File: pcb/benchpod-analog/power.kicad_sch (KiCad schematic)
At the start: 10 parts, among them U30 TPS82130SILR

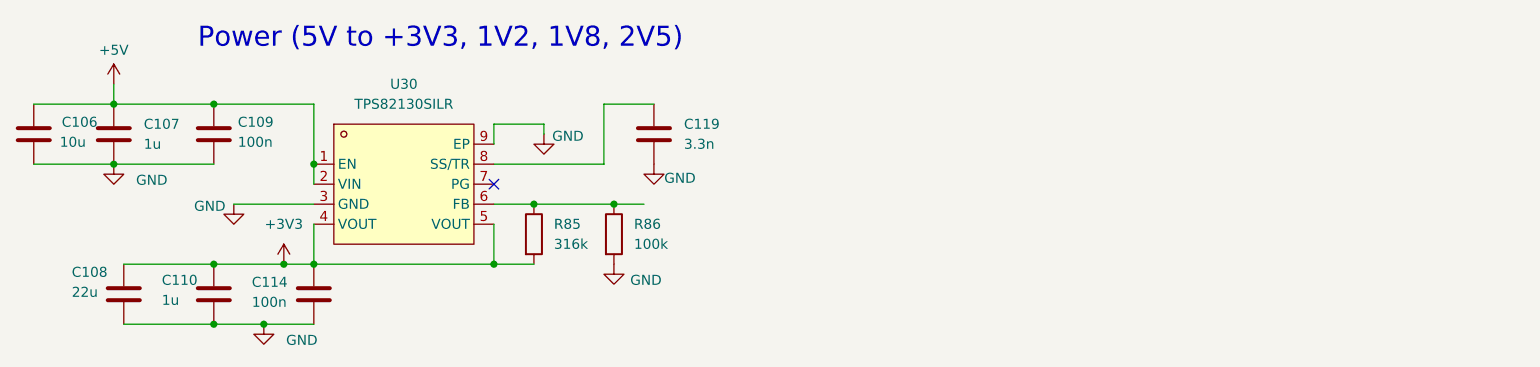
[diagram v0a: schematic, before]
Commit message: analog only board: +3V3 from an AP2112K-3.3 instead of the 3 A buck
On this board +3V3 only feeds logic I/O (DAC8554 IOVDD, MCP33131 DVIO,
TCA9554, the new EEPROM): a few mA. U30 TPS82130 (3 A module) becomes
AP2112K-3.3 (C51118, same part as U46, so no new BOM line): VIN and EN on
+5V, VOUT to +3V3, C107/C109 in, C110/C114 out. R85, R86, C119 and C108
removed. Separate from U46's +3V3A so logic I/O stays off the analog rail.

BOM: TPS82130, 316k and 3.3n lines gone (-3), about $4.75 per board.

Co-Authored-By: Claude Opus 5.5 <noreply@anthropic.com>
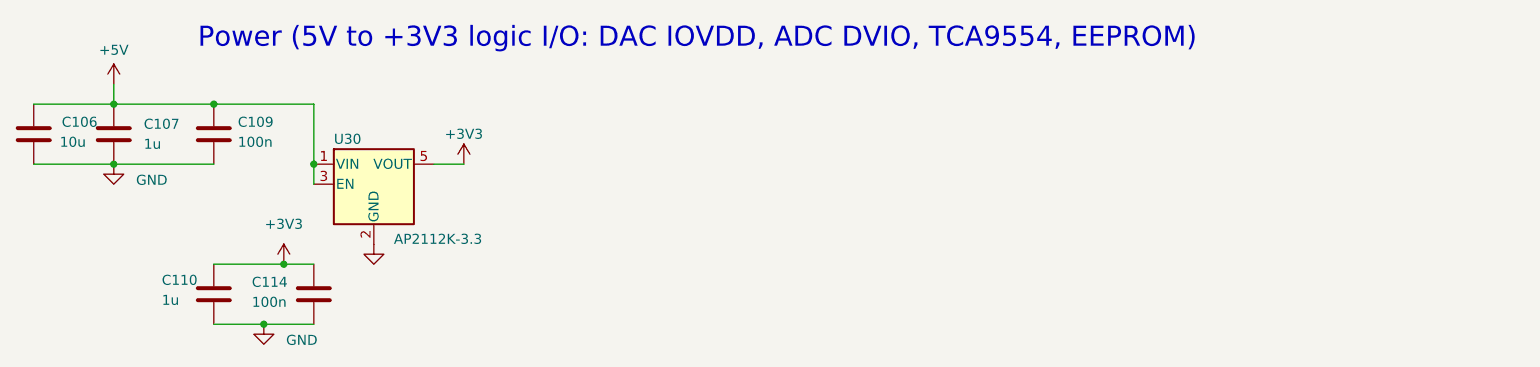
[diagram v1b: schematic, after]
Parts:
- removed C108: 22u, Capacitor_SMD:C_0805_2012Metric, symbol Device:C
- removed C119: 3.3n, Capacitor_SMD:C_0402_1005Metric, symbol Device:C
- removed R85: 316k, Resistor_SMD:R_0402_1005Metric, symbol Device:R
- removed R86: 100k, Resistor_SMD:R_0402_1005Metric, symbol Device:R
- removed U30: TPS82130SILR, lcsc:USIP-8_L3.0-W2.8-P0.65-TL-EP, symbol lcsc_lib:TPS82130SILR
- added U30: AP2112K-3.3, lcsc:SOT-25-5_L2.9-W1.6-P0.95-LS2.8-BL, symbol Regulator_Linear:AP2112K-3.3
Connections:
- net +3V3: now also U30.5 (VOUT)
- net +5V: now also U30.1 (VIN), U30.3 (EN)
- net GND: now also U30.2 (GND)
- no-connect marks 1 -> 0
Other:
- note added: "Power (5V to +3V3 logic I/O: DAC IOVDD, ADC DVIO, TCA9554, EEPROM)"
- note removed: "Power (5V to +3V3, 1V2, 1V8, 2V5)"
